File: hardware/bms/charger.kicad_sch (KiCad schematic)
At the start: 66 parts

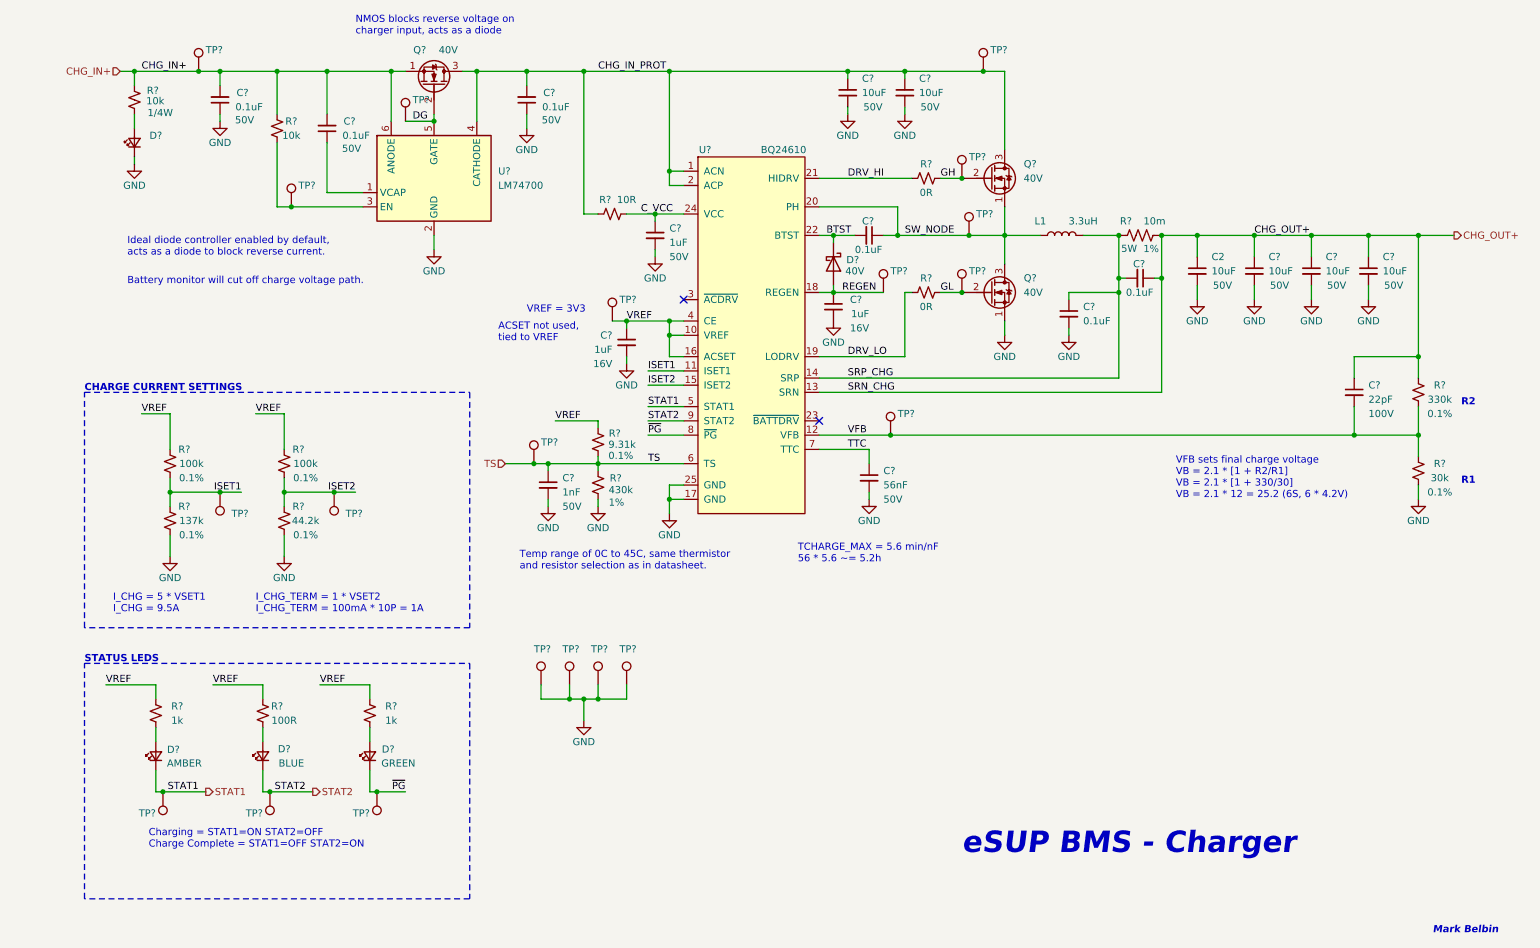
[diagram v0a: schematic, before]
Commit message: Sch mostly complete! Just have the USB C connector left to sort out.
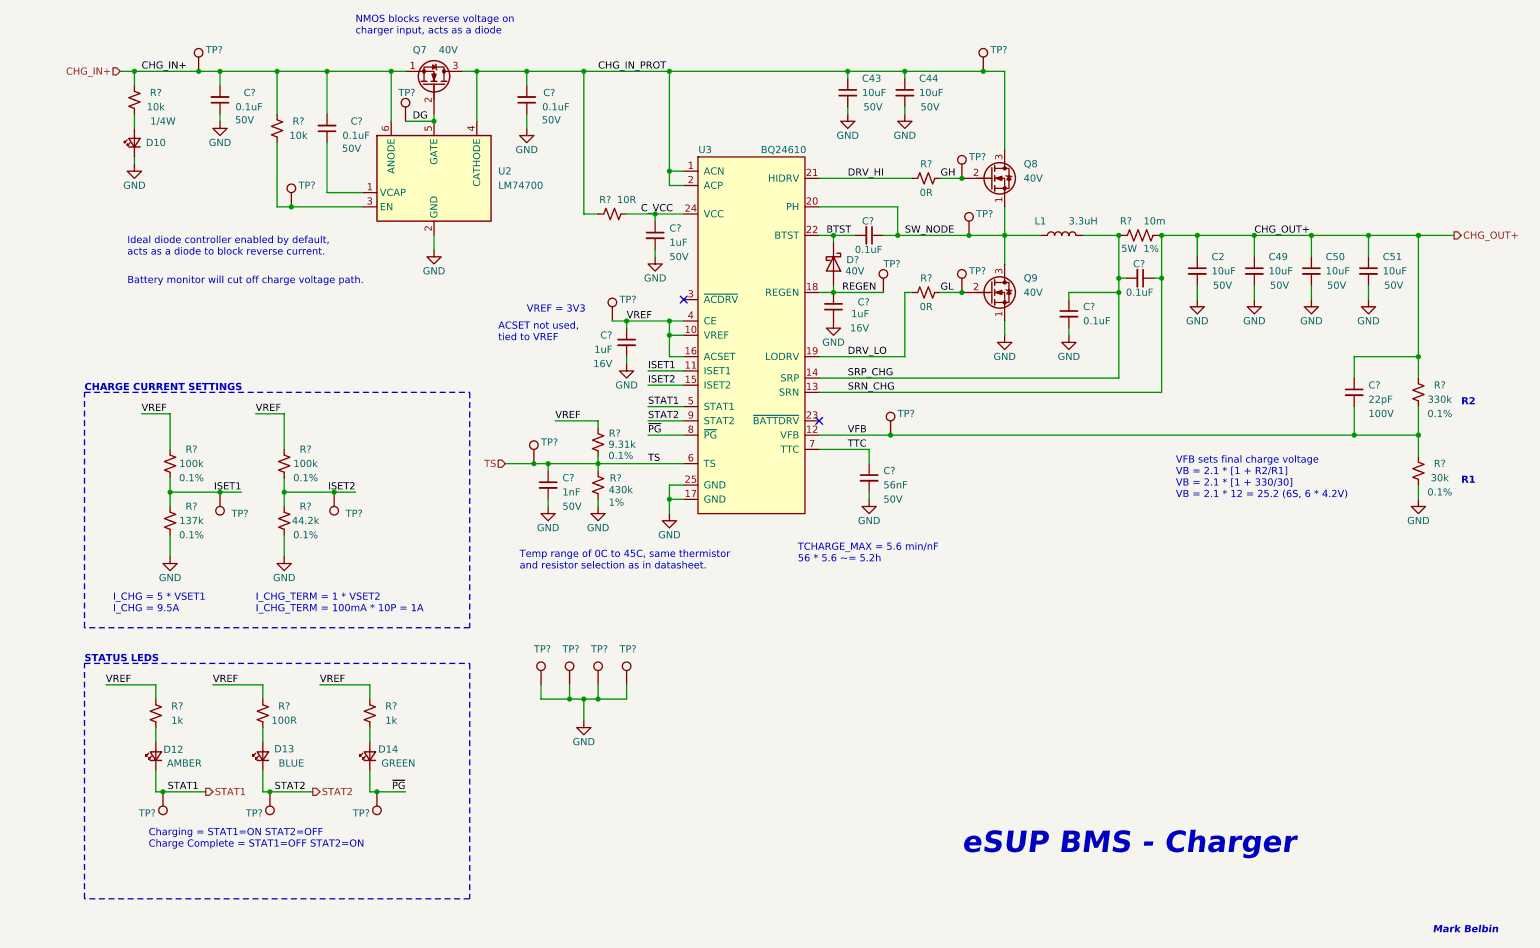
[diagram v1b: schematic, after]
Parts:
- gave numbers to parts that had none: 14
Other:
- title: (none) -> eSUP - Charger

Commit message: Sch cleanup, added extra netties
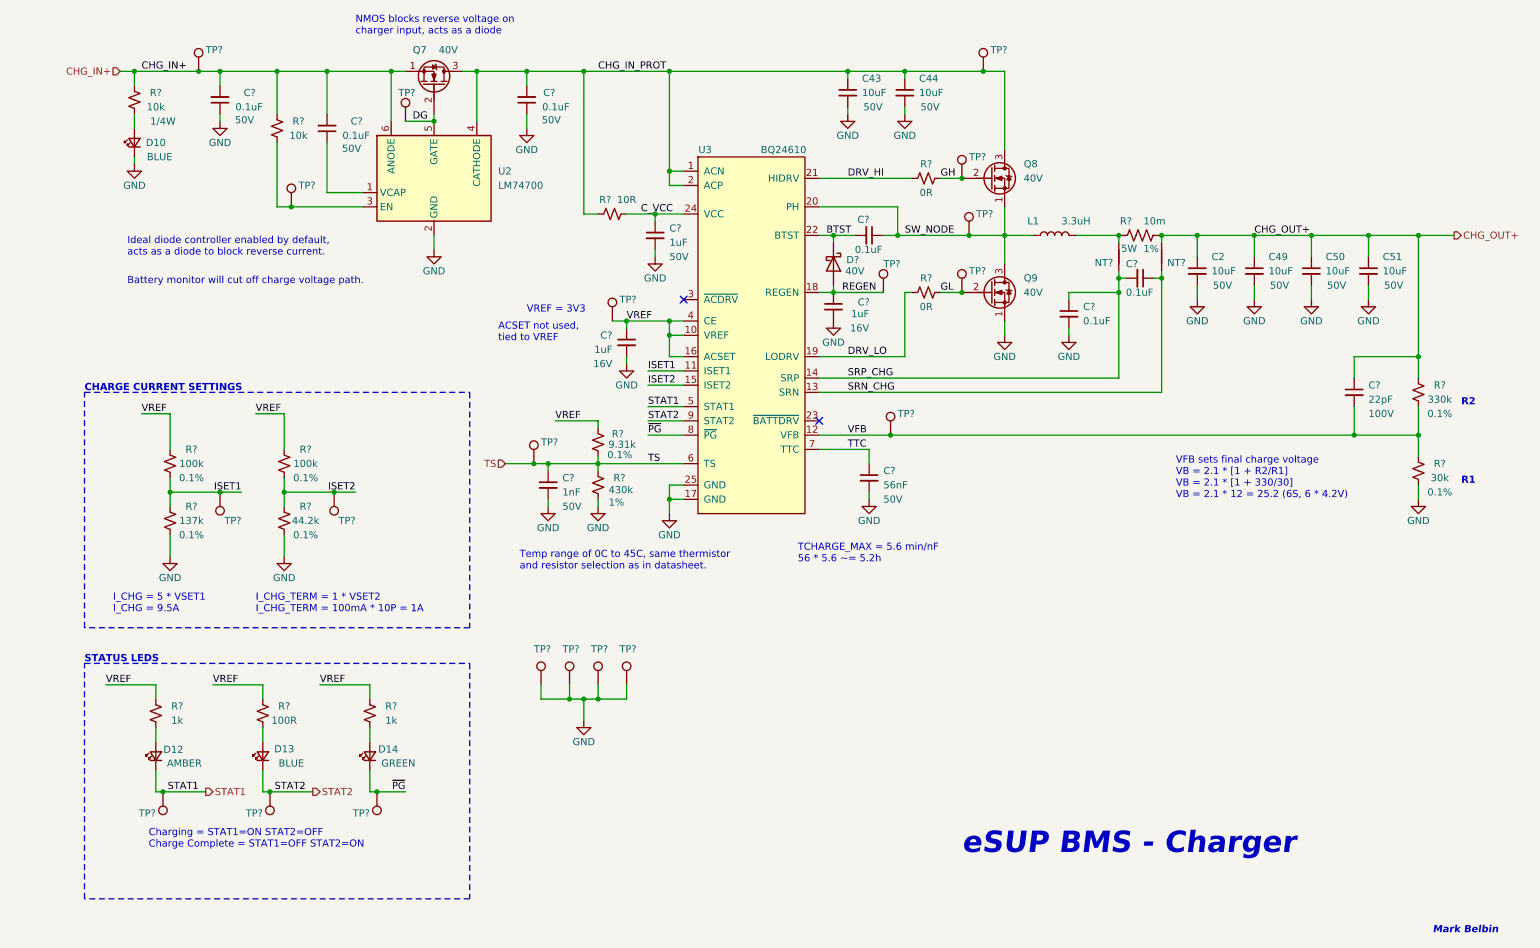
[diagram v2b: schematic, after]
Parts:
- added NT? (x2): Net-Tie, NetTie:NetTie-2_SMD_Pad0.5mm, symbol bms-rescue:Net-Tie_2-Device
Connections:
- net CHG_OUT+: now also NT?.1; no longer C?.1, U3.13 (SRN)
- net SRP_CHG: now also NT?.2; no longer L1.2, R?.2
- new net: L1.2, NT?.1, R?.2
- new net SRN_CHG: C?.1, NT?.2, U3.13 (SRN)
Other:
- moved on the sheet: L1
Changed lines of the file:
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@@
     (stroke (width 0) (type default))
   )
+  (wire (pts (xy 209.55 72.39) (xy 209.55 73.66))
+    (stroke (width 0) (type default))
+  )
   (wire (pts (xy 129.54 113.03) (xy 129.54 115.57))
     (stroke (width 0) (type default))
@@
     (stroke (width 0) (type default))
   )
-  (wire (pts (xy 217.17 66.04) (xy 217.17 73.66))
+  (wire (pts (xy 217.17 66.04) (xy 217.17 67.31))
     (stroke (width 0) (type default))
   )
@@
     (stroke (width 0) (type default))
   )
+  (wire (pts (xy 217.17 72.39) (xy 217.17 73.66))
+    (stroke (width 0) (type default))
+  )
   (wire (pts (xy 177.8 55.88) (xy 181.61 55.88))
     (stroke (width 0) (type default))
@@
     (stroke (width 0) (type default))
   )
-  (wire (pts (xy 203.2 66.04) (xy 209.55 66.04))
+  (wire (pts (xy 201.93 66.04) (xy 209.55 66.04))
     (stroke (width 0) (type default))
   )
@@
     (stroke (width 0) (type default))
   )
-  (wire (pts (xy 209.55 66.04) (xy 209.55 73.66))
+  (wire (pts (xy 209.55 66.04) (xy 209.55 67.31))
     (stroke (width 0) (type default))
   )
@@
     (stroke (width 0) (type default))
   )
-  (wire (pts (xy 189.23 66.04) (xy 195.58 66.04))
+  (wire (pts (xy 189.23 66.04) (xy 194.31 66.04))
     (stroke (width 0) (type default))
   )
@@
   (symbol (lib_id "Device:C_Small") (at 165.1 66.04 270) (unit 1)
     (in_bom yes) (on_board yes) (dnp no)
-    (property "Reference" "C?" (at 163.83 63.5 90)
+    (property "Reference" "C?" (at 163.0155 63.2368 90)
       (effects (font (size 1.27 1.27)) (justify left))
     )
@@
     )
   )
+  (symbol (lib_id "bms-rescue:Net-Tie_2-Device") (at 217.17 69.85 90) (mirror x) (unit 1)
+    (in_bom yes) (on_board yes) (dnp no)
+    (property "Reference" "NT?" (at 221.4654 70.9177 90)
+      (effects (font (size 1.27 1.27)) (justify left))
+    )
+    (property "Value" "Net-Tie" (at 216.0524 70.993 90)
+      (effects (font (size 1.27 1.27)) (justify left) hide)
+    )
+    (property "Footprint" "NetTie:NetTie-2_SMD_Pad0.5mm" (at 217.17 69.85 0)
+      (effects (font (size 1.27 1.27)) hide)
+    )
+    (property "Datasheet" "~" (at 217.17 69.85 0)
+      (effects (font (size 1.27 1.27)) hide)
+    )
+    (pin "1")
+    (pin "2")
+    (instances
+      (project "bms"
+        (path "/a4805e9d-b940-444e-a7cb-db4f4c53ed46"
+          (reference "NT?") (unit 1)
+        )
+        (path "/a4805e9d-b940-444e-a7cb-db4f4c53ed46/00000000-0000-0000-0000-00006523a805"
+          (reference "NT1") (unit 1)
+        )
+        (path "/a4805e9d-b940-444e-a7cb-db4f4c53ed46/00000000-0000-0000-0000-00006523ab32"
+          (reference "NT5") (unit 1)
+        )
+      )
+    )
+  )
   (symbol (lib_id "Device:C_Small") (at 251.46 93.98 0) (unit 1)
     (in_bom yes) (on_board yes) (dnp no)
@@
       (effects (font (size 1.27 1.27)))
     )
-    (property "Value" "BLUE" (at 39.37 50.8 90)
-      (effects (font (size 1.27 1.27)) hide)
+    (property "Value" "BLUE" (at 38.7882 52.07 90)
+      (effects (font (size 1.27 1.27)))
     )
     (property "Footprint" "LED_SMD:LED_0603_1608Metric" (at 34.29 49.53 90)
@@
   (symbol (lib_id "Connector:TestPoint") (at 49.53 111.76 180) (unit 1)
     (in_bom yes) (on_board yes) (dnp no)
-    (property "Reference" "TP?" (at 54.61 115.57 0)
+    (property "Reference" "TP?" (at 53.34 116.84 0)
       (effects (font (size 1.27 1.27)) (justify left))
     )
@@
   (symbol (lib_id "Device:R_Small_US") (at 116.84 110.49 180) (unit 1)
     (in_bom yes) (on_board yes) (dnp no)
-    (property "Reference" "R?" (at 119.9764 109.258 0)
+    (property "Reference" "R?" (at 120.65 109.22 0)
       (effects (font (size 1.27 1.27)))
     )
@@
     )
   )
-  (symbol (lib_id "Device:L") (at 199.39 66.04 90) (unit 1)
+  (symbol (lib_id "Device:L") (at 198.12 66.04 90) (unit 1)
     (in_bom yes) (on_board yes) (dnp no)
-    (property "Reference" "L1" (at 195.58 63.5 90)
+    (property "Reference" "L1" (at 194.31 63.5 90)
       (effects (font (size 1.27 1.27)))
     )
-    (property "Value" "3.3uH" (at 203.2 63.5 90)
+    (property "Value" "3.3uH" (at 201.93 63.5 90)
       (effects (font (size 1.27 1.27)))
     )
-    (property "Footprint" "bms:HCM1307-3R3-R" (at 199.39 66.04 0)
+    (property "Footprint" "bms:HCM1307-3R3-R" (at 198.12 66.04 0)
       (effects (font (size 1.27 1.27)) hide)
     )
-    (property "Datasheet" "~" (at 199.39 66.04 0)
+    (property "Datasheet" "~" (at 198.12 66.04 0)
       (effects (font (size 1.27 1.27)) hide)
     )
-    (property "MFG" "Eaton - Electronics Division" (at 199.39 66.04 90)
+    (property "MFG" "Eaton - Electronics Division" (at 198.12 66.04 90)
       (effects (font (size 1.27 1.27)) hide)
     )
-    (property "MFG PN" "HCM1307-3R3-R" (at 199.39 66.04 90)
+    (property "MFG PN" "HCM1307-3R3-R" (at 198.12 66.04 90)
       (effects (font (size 1.27 1.27)) hide)
     )
-    (property "DCR" "4.5m" (at 199.39 66.04 90)
+    (property "DCR" "4.5m" (at 198.12 66.04 90)
       (effects (font (size 1.27 1.27)) hide)
     )
-    (property "Imax" "15A" (at 199.39 66.04 90)
+    (property "Imax" "15A" (at 198.12 66.04 90)
       (effects (font (size 1.27 1.27)) hide)
     )
@@
   (symbol (lib_id "Device:R_Small_US") (at 116.84 102.87 180) (unit 1)
     (in_bom yes) (on_board yes) (dnp no)
-    (property "Reference" "R?" (at 119.808 101.2761 0)
+    (property "Reference" "R?" (at 120.3488 101.3855 0)
       (effects (font (size 1.27 1.27)))
     )
@@
       (effects (font (size 1.27 1.27)) hide)
     )
-    (property "Tolerance" "0.1%" (at 120.8857 105.2502 0)
+    (property "Tolerance" "0.1%" (at 120.6979 105.1088 0)
       (effects (font (size 1.27 1.27)))
     )
@@
     )
   )
+  (symbol (lib_id "bms-rescue:Net-Tie_2-Device") (at 209.55 69.85 270) (unit 1)
+    (in_bom yes) (on_board yes) (dnp no)
+    (property "Reference" "NT?" (at 205.2546 70.9177 90)
+      (effects (font (size 1.27 1.27)) (justify left))
+    )
+    (property "Value" "Net-Tie" (at 210.6676 70.993 90)
+      (effects (font (size 1.27 1.27)) (justify left) hide)
+    )
+    (property "Footprint" "NetTie:NetTie-2_SMD_Pad0.5mm" (at 209.55 69.85 0)
+      (effects (font (size 1.27 1.27)) hide)
+    )
+    (property "Datasheet" "~" (at 209.55 69.85 0)
+      (effects (font (size 1.27 1.27)) hide)
+    )
+    (pin "1")
+    (pin "2")
+    (instances
+      (project "bms"
+        (path "/a4805e9d-b940-444e-a7cb-db4f4c53ed46"
+          (reference "NT?") (unit 1)
+        )
+        (path "/a4805e9d-b940-444e-a7cb-db4f4c53ed46/00000000-0000-0000-0000-00006523a805"
+          (reference "NT1") (unit 1)
+        )
+        (path "/a4805e9d-b940-444e-a7cb-db4f4c53ed46/00000000-0000-0000-0000-00006523ab32"
+          (reference "NT4") (unit 1)
+        )
+      )
+    )
+  )
   (symbol (lib_id "power:GND") (at 114.3 152.4 0) (unit 1)
     (in_bom yes) (on_board yes) (dnp no)
@@
   (symbol (lib_id "Device:C_Small") (at 213.36 73.66 270) (unit 1)
     (in_bom yes) (on_board yes) (dnp no)
-    (property "Reference" "C?" (at 212.09 71.12 90)
+    (property "Reference" "C?" (at 210.82 71.12 90)
       (effects (font (size 1.27 1.27)) (justify left))
     )
@@
   (symbol (lib_id "Connector:TestPoint") (at 69.85 111.76 180) (unit 1)
     (in_bom yes) (on_board yes) (dnp no)
-    (property "Reference" "TP?" (at 74.93 115.57 0)
+    (property "Reference" "TP?" (at 73.66 116.84 0)
       (effects (font (size 1.27 1.27)) (justify left))
     )

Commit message: Continued layout, defined board area based on mech assembly
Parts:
- L1: footprint bms:HCM1307-3R3-R -> bms:IND_ETQP5M3R3YFK; DCR 4.5m -> 10.45m; Imax 15A -> 12.5A; MFG Eaton - Electronics Division -> Panasonic Electronic Components; MFG PN HCM1307-3R3-R -> ETQ-P5M3R3YFK
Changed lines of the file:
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@@
       (effects (font (size 1.27 1.27)))
     )
-    (property "Footprint" "bms:HCM1307-3R3-R" (at 198.12 66.04 0)
+    (property "Footprint" "bms:IND_ETQP5M3R3YFK" (at 198.12 66.04 0)
       (effects (font (size 1.27 1.27)) hide)
     )
@@
       (effects (font (size 1.27 1.27)) hide)
     )
-    (property "MFG" "Eaton - Electronics Division" (at 198.12 66.04 90)
+    (property "MFG" "Panasonic Electronic Components" (at 198.12 66.04 90)
       (effects (font (size 1.27 1.27)) hide)
     )
-    (property "MFG PN" "HCM1307-3R3-R" (at 198.12 66.04 90)
+    (property "MFG PN" "ETQ-P5M3R3YFK" (at 198.12 66.04 90)
       (effects (font (size 1.27 1.27)) hide)
     )
-    (property "DCR" "4.5m" (at 198.12 66.04 90)
+    (property "DCR" "10.45m" (at 198.12 66.04 90)
       (effects (font (size 1.27 1.27)) hide)
     )
-    (property "Imax" "15A" (at 198.12 66.04 90)
+    (property "Imax" "12.5A" (at 198.12 66.04 90)
       (effects (font (size 1.27 1.27)) hide)
     )

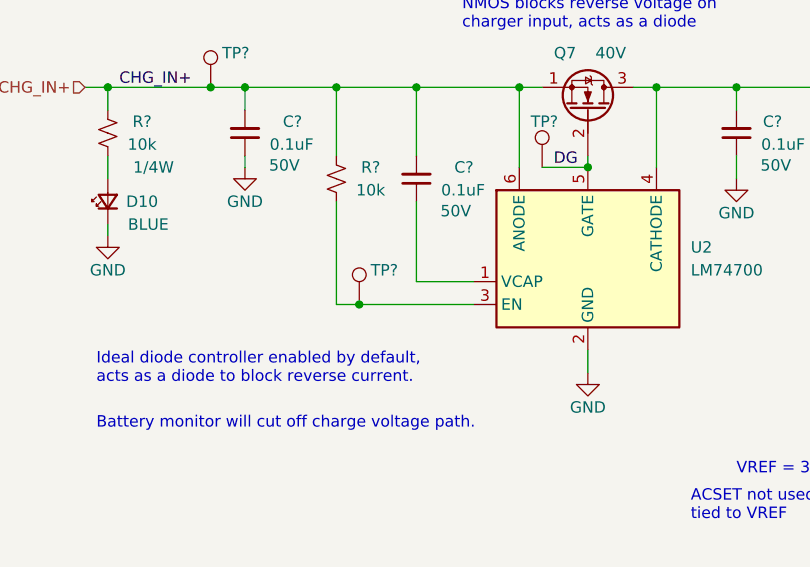
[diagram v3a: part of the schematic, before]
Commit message: Updated test points to 0.5mm to save space, continued layout
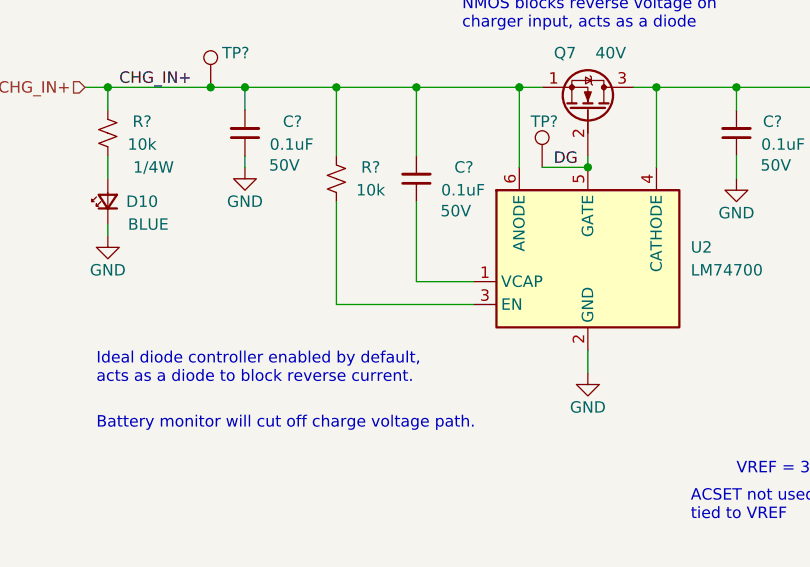
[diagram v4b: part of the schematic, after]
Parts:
- removed TP?: TestPoint, TestPoint:TestPoint_Pad_D1.0mm, symbol Connector:TestPoint
- NT? (x2): now left out of the parts list
- TP? (x19): footprint TestPoint:TestPoint_Pad_D1.0mm -> bms:TestPoint_Pad_D0.5mm; now left out of the parts list

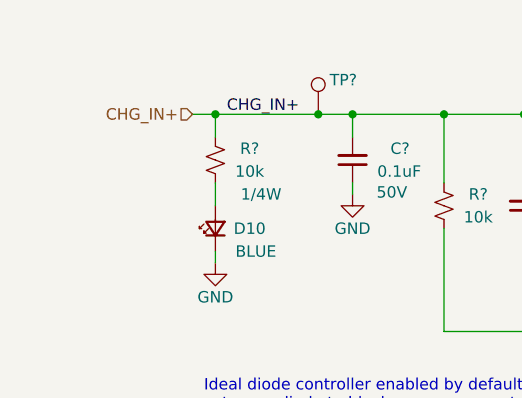
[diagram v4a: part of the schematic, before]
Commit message: More layout, changed precharge / predischarged PMOS selection to SOT-23 size to save space. Charger layout will be difficult, may need to change charger input terminal location...
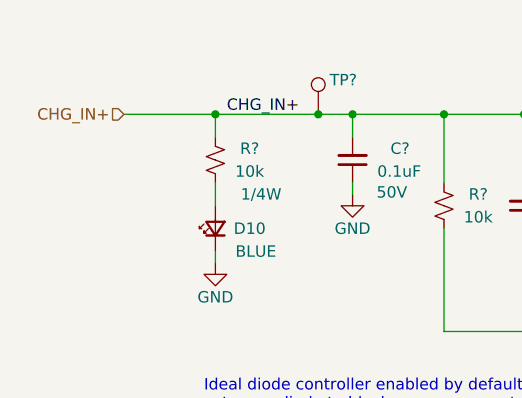
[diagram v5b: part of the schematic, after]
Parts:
- NT? (x2): footprint NetTie:NetTie-2_SMD_Pad0.5mm -> bms:NetTie-2_SMD_Pad_8mil
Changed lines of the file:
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@@
     (stroke (width 0) (type default))
   )
-  (wire (pts (xy 31.75 36.83) (xy 34.29 36.83))
+  (wire (pts (xy 24.13 36.83) (xy 34.29 36.83))
     (stroke (width 0) (type default))
   )
@@
     (effects (font (size 1.27 1.27)) (justify left bottom))
   )
-  (hierarchical_label "CHG_IN+" (shape input) (at 31.75 36.83 180) (fields_autoplaced)
+  (hierarchical_label "CHG_IN+" (shape input) (at 24.13 36.83 180) (fields_autoplaced)
     (effects (font (size 1.27 1.27)) (justify right))
   )
@@
       (effects (font (size 1.27 1.27)) (justify left) hide)
     )
-    (property "Footprint" "NetTie:NetTie-2_SMD_Pad0.5mm" (at 217.17 69.85 0)
+    (property "Footprint" "bms:NetTie-2_SMD_Pad_8mil" (at 217.17 69.85 0)
       (effects (font (size 1.27 1.27)) hide)
     )
@@
       (effects (font (size 1.27 1.27)) (justify left) hide)
     )
-    (property "Footprint" "NetTie:NetTie-2_SMD_Pad0.5mm" (at 209.55 69.85 0)
-      (effects (font (size 1.27 1.27)) hide)
-    )
+    (property "Footprint" "bms:NetTie-2_SMD_Pad_8mil" (at 209.55 69.85 0)
+      (effects (font (size 1.27 1.27)) hide)
+    )
